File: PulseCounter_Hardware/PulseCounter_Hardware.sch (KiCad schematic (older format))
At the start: 5 parts, among them U5 LTV-817

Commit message: Starting with MCU
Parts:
- removed D1: 151033RS03000, digikey-footprints:LED_3mm_Radial, symbol dk_LED-Indication-Discrete:151033RS03000
- removed R1, R2: 1K, symbol Device:R
- removed RV1: Varistor, symbol Device:Varistor
- removed U5: LTV-817, digikey-footprints:DIP-4_W7.62mm, symbol dk_Optoisolators-Transistor-Photovoltaic-Output:LTV-817
- added JP?: Jumper_2_Open, symbol Jumper:Jumper_2_Open
- added R?: R, symbol Device:R
- added U66: STM32F103C8Tx, Package_QFP:LQFP-48_7x7mm_P0.5mm, symbol MCU_ST_STM32F1:STM32F103C8Tx
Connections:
- net 3V3: now also R?.1, U66.24 (VDD), U66.36 (VDD), U66.48 (VDD), U66.9 (VDDA)
- net GND: now also U66.23 (VSS), U66.35 (VSS), U66.47 (VSS), U66.8 (VSSA)
- new net: R?.2, U66.7 (NRST)
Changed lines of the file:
@@
 Comment4 ""
 $EndDescr
-$Comp
-L dk_Optoisolators-Transistor-Photovoltaic-Output:LTV-817 U5
-U 1 1 5F6C991F
-P 10000 1800
-F 0 "U5" H 10000 2147 60  0000 C CNN
-F 1 "LTV-817" H 10000 2041 60  0000 C CNN
-F 2 "digikey-footprints:DIP-4_W7.62mm" V 10200 2000 60  0001 L CNN
-F 3 "http://optoelectronics.liteon.com/upload/download/DS-70-96-0016/LTV-8X7%20series%20201610%20.pdf" V 10200 2100 60  0001 L CNN
-F 4 "160-1366-5-ND" H 10200 2200 60  0001 L CNN "Digi-Key_PN"
-F 5 "LTV-817" H 10200 2300 60  0001 L CNN "MPN"
-F 6 "Isolators" H 10200 2400 60  0001 L CNN "Category"
-F 7 "Optoisolators - Transistor, Photovoltaic Output" H 10200 2500 60  0001 L CNN "Family"
-F 8 "http://optoelectronics.liteon.com/upload/download/DS-70-96-0016/LTV-8X7%20series%20201610%20.pdf" H 10200 2600 60  0001 L CNN "DK_Datasheet_Link"
-F 9 "/product-detail/en/lite-on-inc/LTV-817/160-1366-5-ND/385836" H 10200 2700 60  0001 L CNN "DK_Detail_Page"
-F 10 "OPTOISOLATR 5KV TRANSISTOR 4-DIP" H 10200 2800 60  0001 L CNN "Description"
-F 11 "Lite-On Inc." H 10200 2900 60  0001 L CNN "Manufacturer"
-F 12 "Active" H 10200 3000 60  0001 L CNN "Status"
-	1    10000 1800
-	1    0    0    -1
-$EndComp
-$Comp
-L Device:R R1
-U 1 1 5F6D6399
-P 9550 1700
-F 0 "R1" V 9343 1700 50  0000 C CNN
-F 1 "1K" V 9434 1700 50  0000 C CNN
-F 2 "" V 9480 1700 50  0001 C CNN
-F 3 "~" H 9550 1700 50  0001 C CNN
-	1    9550 1700
-	0    1    1    0
-$EndComp
-$Comp
-L Device:Varistor RV1
-U 1 1 5F6D6B52
-P 9150 1850
-F 0 "RV1" H 9200 1900 50  0000 L CNN
-F 1 "Varistor" H 9200 1750 50  0000 L CNN
-F 2 "" V 9080 1850 50  0001 C CNN
-F 3 "~" H 9150 1850 50  0001 C CNN
-	1    9150 1850
-	1    0    0    -1
-$EndComp
-Wire Wire Line
-	9150 1700 9400 1700
-$Comp
-L dk_LED-Indication-Discrete:151033RS03000 D1
-U 1 1 5F6D8142
-P 8900 1700
-F 0 "D1" H 8850 2037 60  0000 C CNN
-F 1 "151033RS03000" H 8850 1931 60  0000 C CNN
-F 2 "digikey-footprints:LED_3mm_Radial" H 9100 1900 60  0001 L CNN
-F 3 "https://katalog.we-online.de/led/datasheet/151033RS03000.pdf" H 9100 2000 60  0001 L CNN
-F 4 "732-5013-ND" H 9100 2100 60  0001 L CNN "Digi-Key_PN"
-F 5 "151033RS03000" H 9100 2200 60  0001 L CNN "MPN"
-F 6 "Optoelectronics" H 9100 2300 60  0001 L CNN "Category"
-F 7 "LED Indication - Discrete" H 9100 2400 60  0001 L CNN "Family"
-F 8 "https://katalog.we-online.de/led/datasheet/151033RS03000.pdf" H 9100 2500 60  0001 L CNN "DK_Datasheet_Link"
-F 9 "/product-detail/en/wurth-electronics-inc/151033RS03000/732-5013-ND/4490003" H 9100 2600 60  0001 L CNN "DK_Detail_Page"
-F 10 "LED RED CLEAR 3MM ROUND T/H" H 9100 2700 60  0001 L CNN "Description"
-F 11 "Wurth Electronics Inc." H 9100 2800 60  0001 L CNN "Manufacturer"
-F 12 "Active" H 9100 2900 60  0001 L CNN "Status"
-	1    8900 1700
-	1    0    0    -1
-$EndComp
-Wire Wire Line
-	9000 1700 9150 1700
-Connection ~ 9150 1700
-Text Label 8700 1700 2    50   ~ 0
-CHANNEL_IN_0
-$Comp
-L Device:R R2
-U 1 1 5F6E3A2D
-P 10300 1550
-F 0 "R2" H 10230 1504 50  0000 R CNN
-F 1 "1K" H 10230 1595 50  0000 R CNN
-F 2 "" V 10230 1550 50  0001 C CNN
-F 3 "~" H 10300 1550 50  0001 C CNN
-	1    10300 1550
-	-1   0    0    1
-$EndComp
-Text Label 10450 1700 3    50   ~ 0
-CHANNEL_OUT_0
-Connection ~ 10300 1700
-Wire Wire Line
-	10300 2150 10300 1900
-Text Label 10300 1400 2    50   ~ 0
-3V3
-Text Label 9450 2050 3    50   ~ 0
-OPTO_GND
-Text Label 10300 2150 3    50   ~ 0
-GND
-Wire Wire Line
-	9150 2000 9450 2000
-Wire Wire Line
-	9700 2000 9700 1900
-Wire Wire Line
-	9450 2050 9450 2000
-Connection ~ 9450 2000
-Wire Wire Line
-	9450 2000 9700 2000
-Wire Wire Line
-	10300 1700 10450 1700
 $Sheet
 S 14600 4650 900  650
@@
 F13 "NCCLR" I R 15500 5000 50
 $EndSheet
+$Comp
+L MCU_ST_STM32F1:STM32F103C8Tx U66
+U 1 1 5FD147D4
+P 10250 5800
+F 0 "U66" H 10200 4000 50  0000 C CNN
+F 1 "STM32F103C8Tx" H 10250 3900 50  0000 C CNN
+F 2 "Package_QFP:LQFP-48_7x7mm_P0.5mm" H 9650 4400 50  0001 R CNN
+F 3 "http://www.st.com/st-web-ui/static/active/en/resource/technical/document/datasheet/CD00161566.pdf" H 10250 5800 50  0001 C CNN
+	1    10250 5800
+	1    0    0    -1
+$EndComp
+Text Label 10150 7300 3    50   ~ 0
+GND
+Text Label 10050 7300 3    50   ~ 0
+GND
+Text Label 10250 7300 3    50   ~ 0
+GND
+Text Label 10350 7300 3    50   ~ 0
+GND
+Text Label 10150 4300 1    50   ~ 0
+3V3
+Text Label 10250 4300 1    50   ~ 0
+3V3
+Text Label 10350 4300 1    50   ~ 0
+3V3
+Text Label 10450 4300 1    50   ~ 0
+3V3
+Text Label 9450 4150 1    50   ~ 0
+3V3
+$Comp
+L Device:R R?
+U 1 1 5FDF826F
+P 9450 4350
+F 0 "R?" H 9520 4396 50  0000 L CNN
+F 1 "R" H 9520 4305 50  0000 L CNN
+F 2 "" V 9380 4350 50  0001 C CNN
+F 3 "~" H 9450 4350 50  0001 C CNN
+	1    9450 4350
+	1    0    0    -1
+$EndComp
+Wire Wire Line
+	9450 4500 9550 4500
+Wire Wire Line
+	9450 4200 9450 4150
+$Comp
+L Jumper:Jumper_2_Open JP?
+U 1 1 5F6DFD0C
+P 9100 4700
+F 0 "JP?" H 9100 4935 50  0000 C CNN
+F 1 "Jumper_2_Open" H 9100 4844 50  0000 C CNN
+F 2 "" H 9100 4700 50  0001 C CNN
+F 3 "~" H 9100 4700 50  0001 C CNN
+	1    9100 4700
+	1    0    0    -1
+$EndComp
 $EndSCHEMATC

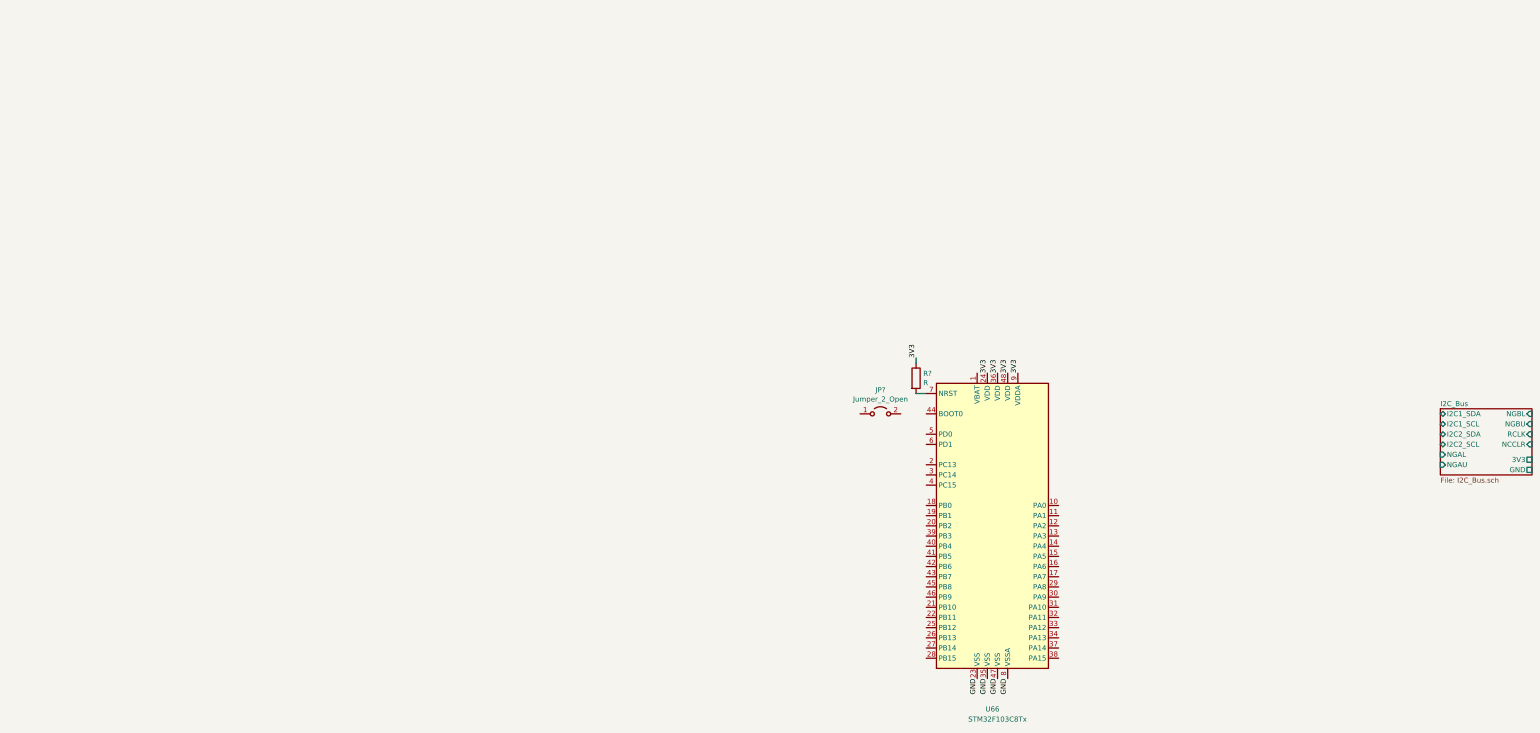
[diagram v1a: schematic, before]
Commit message: Added SPI flash, connected I2C, SPI
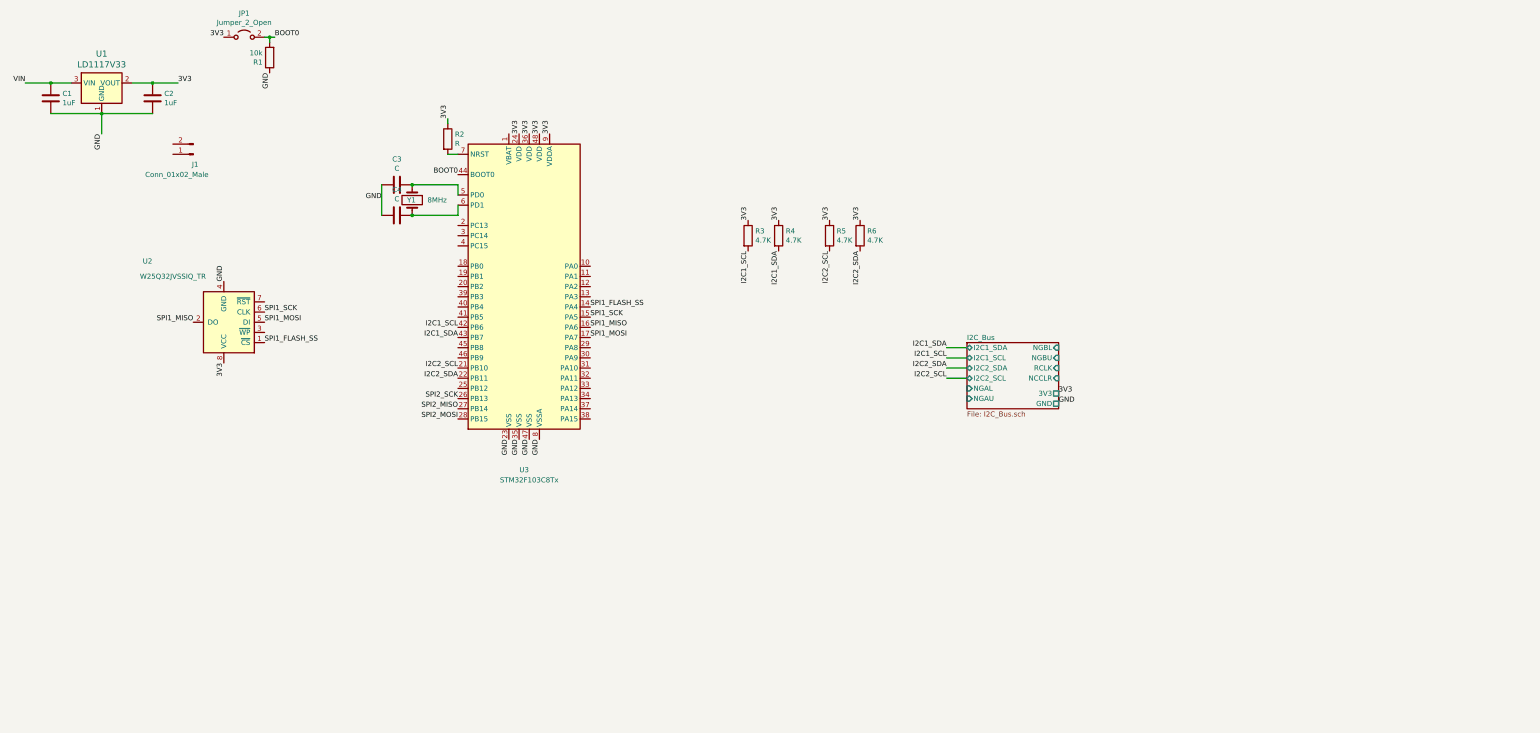
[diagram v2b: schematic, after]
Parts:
- added C1, C2: 1uF, symbol Device:C
- added C3, C4: C, symbol Device:C
- added J1: Conn_01x02_Male, symbol Connector:Conn_01x02_Male
- added R1: 10k, symbol Device:R
- added R3, R4, R5, R6: 4.7K, symbol Device:R
- added U1: LD1117V33, digikey-footprints:TO-220-3, symbol dk_PMIC-Voltage-Regulators-Linear:LD1117V33
- added U2: W25Q32JVSSIQ_TR, digikey-footprints:SOIC-8_W5.6mm, symbol dk_Memory:W25Q32JVSSIQ_TR
- added Y1: 8MHz, symbol Device:Crystal
- gave numbers to parts that had none: 2
- renumbered U66 to U3
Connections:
- net 3V3: now also JP1.1 (A), C2.1, R3.1, R4.1, R5.1, R6.1, U1.2 (VOUT), U2.8 (VCC)
- net GND: now also C1.2, C2.2, C3.1, C4.1, R1.1, U1.1 (GND), U2.4 (GND)
- net BOOT0: now reaches JP1.2 (B)
- net BOOT0: now also U3.44 (BOOT0), R1.2
- net SPI1_FLASH_SS: now reaches U3.14 (PA4)
- net SPI1_FLASH_SS: now also U2.1 (~CS)
- net SPI1_SCK: now reaches U3.15 (PA5)
- net SPI1_SCK: now also U2.6 (CLK)
- net SPI1_MISO: now reaches U3.16 (PA6)
- net SPI1_MISO: now also U2.2 (DO)
- net SPI1_MOSI: now reaches U3.17 (PA7)
- net SPI1_MOSI: now also U2.5 (DI)
- net I2C2_SCL: now reaches U3.21 (PB10)
- net I2C2_SCL: now also R5.2
- net I2C2_SDA: now reaches U3.22 (PB11)
- net I2C2_SDA: now also R6.2
- net SPI2_SCK: now reaches U3.26 (PB13)
- net SPI2_MISO: now reaches U3.27 (PB14)
- net SPI2_MOSI: now reaches U3.28 (PB15)
- net I2C1_SCL: now reaches U3.42 (PB6)
- net I2C1_SCL: now also R3.2
- net I2C1_SDA: now reaches U3.43 (PB7)
- net I2C1_SDA: now also R4.2
- net at U3.5 (PD0): now also C3.2, Y1.1
- net at U3.6 (PD1): now also C4.2, Y1.2
- new net VIN: C1.1, U1.3 (VIN)
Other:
- moved on the sheet: JP1, R2, U3

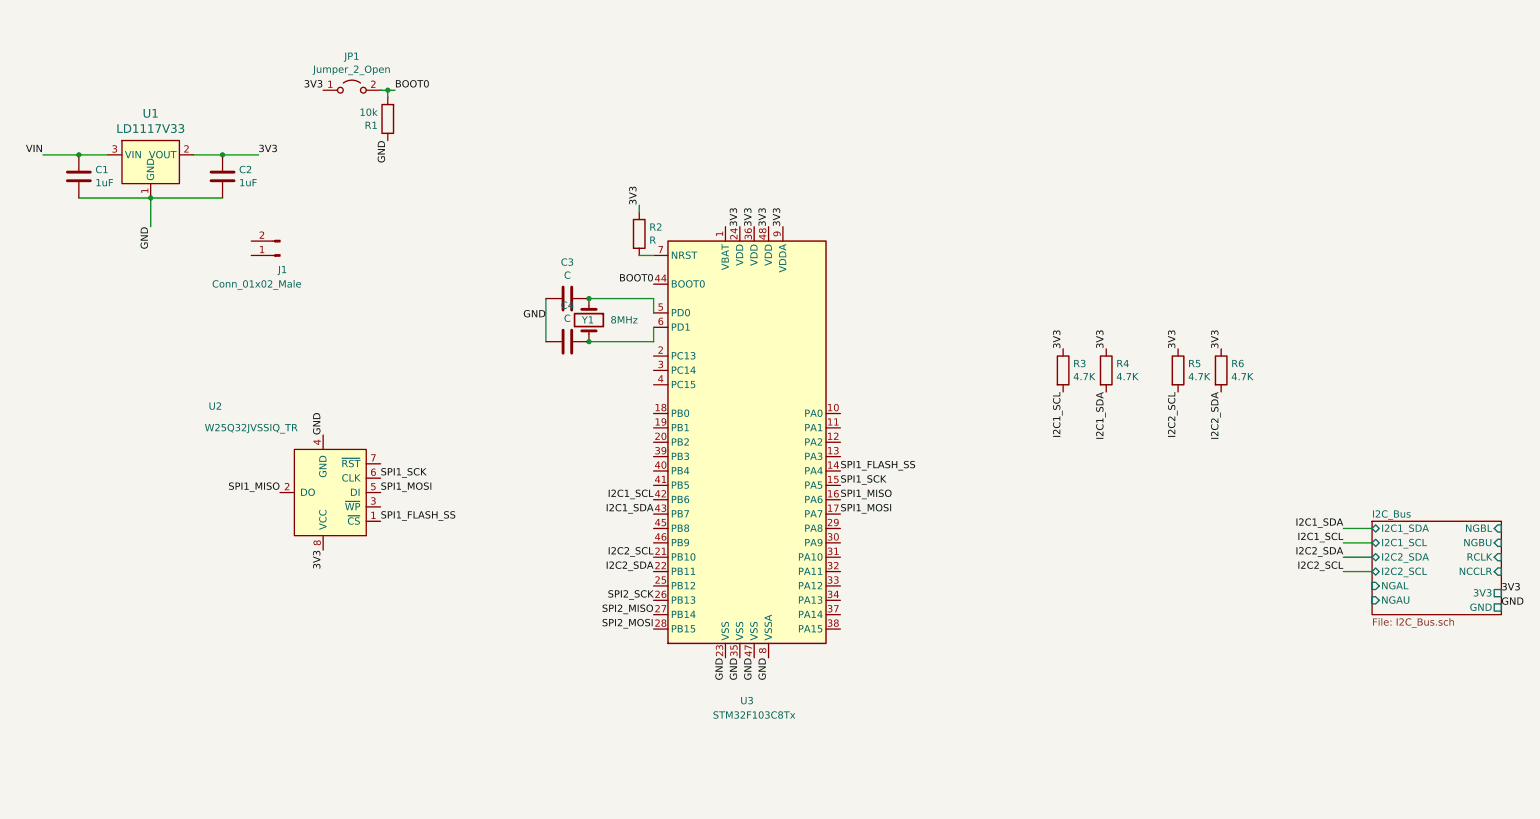
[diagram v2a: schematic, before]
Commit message: Added correct varistor
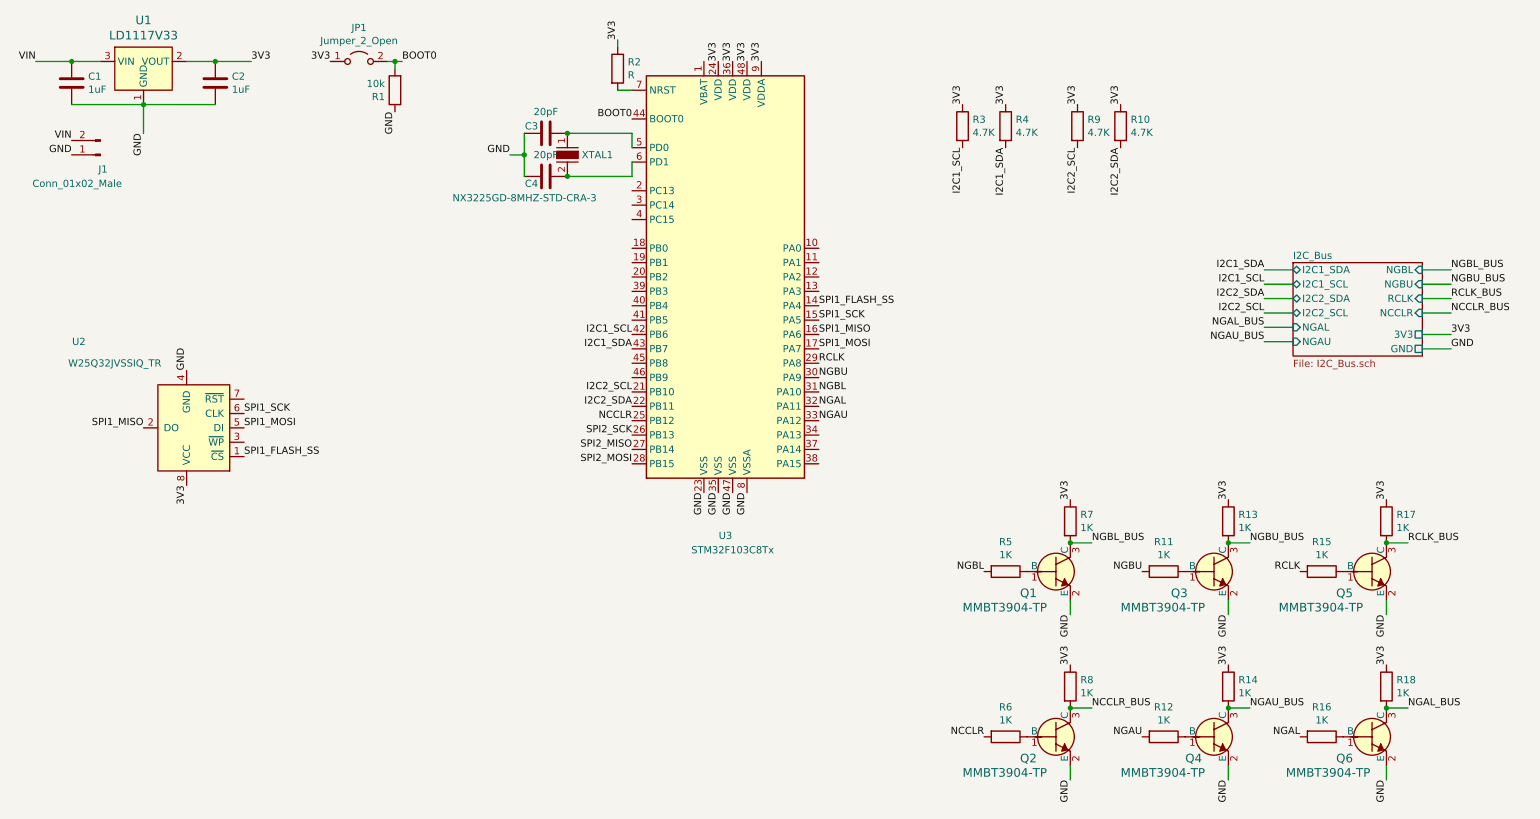
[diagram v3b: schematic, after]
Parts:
- removed Y1: 8MHz, symbol Device:Crystal
- added Q1, Q2, Q3, Q4, Q5, Q6: MMBT3904-TP, digikey-footprints:SOT-23-3, symbol dk_Transistors-Bipolar-BJT-Single:MMBT3904-TP
- added R11, R12, R13, R14, R15, R16, R17, R18, R5, R6, R7, R8: 1K, Resistor_SMD:R_0603_1608Metric_Pad1.05x0.95mm_HandSolder, symbol Device:R
- added XTAL1: NX3225GD-8MHZ-STD-CRA-3, digikey-footprints:SMD-2_3.2x2.5mm, symbol dk_Crystals:NX3225GD-8MHZ-STD-CRA-3
- C1, C2: footprint (none) -> Capacitor_SMD:C_0603_1608Metric_Pad1.05x0.95mm_HandSolder
- C3, C4: value C -> 20pF; footprint (none) -> Capacitor_SMD:C_0603_1608Metric_Pad1.05x0.95mm_HandSolder
- J1, JP1: footprint (none) -> Connector_PinSocket_2.54mm:PinSocket_1x02_P2.54mm_Vertical
- R1, R2, R3, R4: footprint (none) -> Resistor_SMD:R_0603_1608Metric_Pad1.05x0.95mm_HandSolder
- R10: renamed from R6; footprint (none) -> Resistor_SMD:R_0603_1608Metric_Pad1.05x0.95mm_HandSolder
- R9: renamed from R5; footprint (none) -> Resistor_SMD:R_0603_1608Metric_Pad1.05x0.95mm_HandSolder
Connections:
- net 3V3: now also R13.1, R14.1, R17.1, R18.1, R7.1, R8.1
- net GND: now also J1.1 (Pin_1), Q1.2 (E), Q2.2 (E), Q3.2 (E), Q4.2 (E), Q5.2 (E), Q6.2 (E)
- net VIN: now also J1.2 (Pin_2)
- net at C3.2, U3.5 (PD0): now also XTAL1.1
- net at C4.2, U3.6 (PD1): now also XTAL1.2
- net NCCLR: now reaches U3.25 (PB12)
- net NCCLR: now also R6.2
- net RCLK: now reaches U3.29 (PA8)
- net RCLK: now also R15.2
- net NGBU: now reaches U3.30 (PA9)
- net NGBU: now also R11.2
- net NGBL: now reaches U3.31 (PA10)
- net NGBL: now also R5.2
- net NGAL: now reaches U3.32 (PA11)
- net NGAL: now also R16.2
- net NGAU: now reaches U3.33 (PA12)
- net NGAU: now also R12.2
- new net: Q3.1 (B), R11.1
- new net: Q5.1 (B), R15.1
- new net: Q4.1 (B), R12.1
- new net: Q6.1 (B), R16.1
- new net: Q1.1 (B), R5.1
- new net: Q2.1 (B), R6.1
- new net NCCLR_BUS: Q2.3 (C), R8.2
- new net NGAL_BUS: Q6.3 (C), R18.2
- new net NGAU_BUS: Q4.3 (C), R14.2
- new net NGBL_BUS: Q1.3 (C), R7.2
- new net NGBU_BUS: Q3.3 (C), R13.2
- new net RCLK_BUS: Q5.3 (C), R17.2
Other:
- moved on the sheet: C1, C2, C3, C4, J1, JP1, R1, R10, R2, R3, R4, R9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
